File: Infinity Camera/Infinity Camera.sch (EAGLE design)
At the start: 6 parts

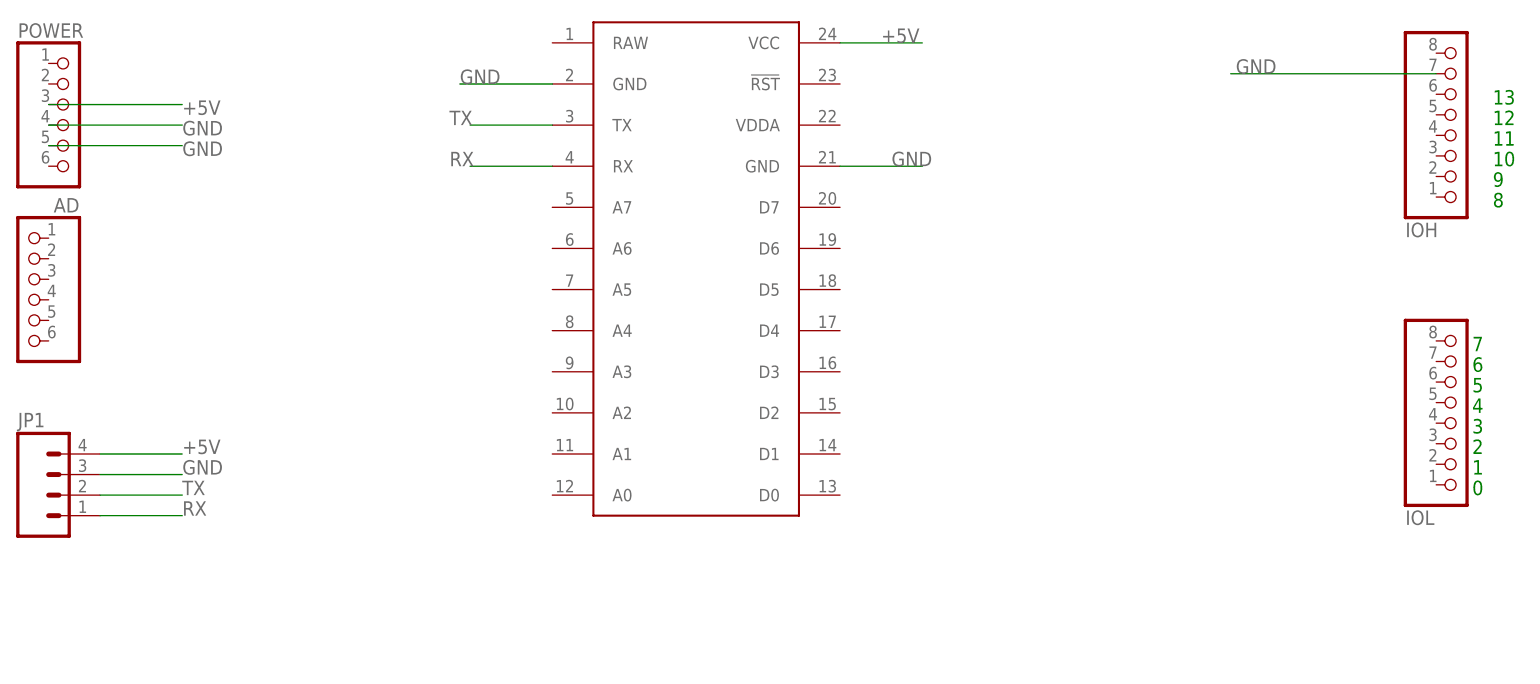
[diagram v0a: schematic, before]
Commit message: Reviewed Infinity Camera
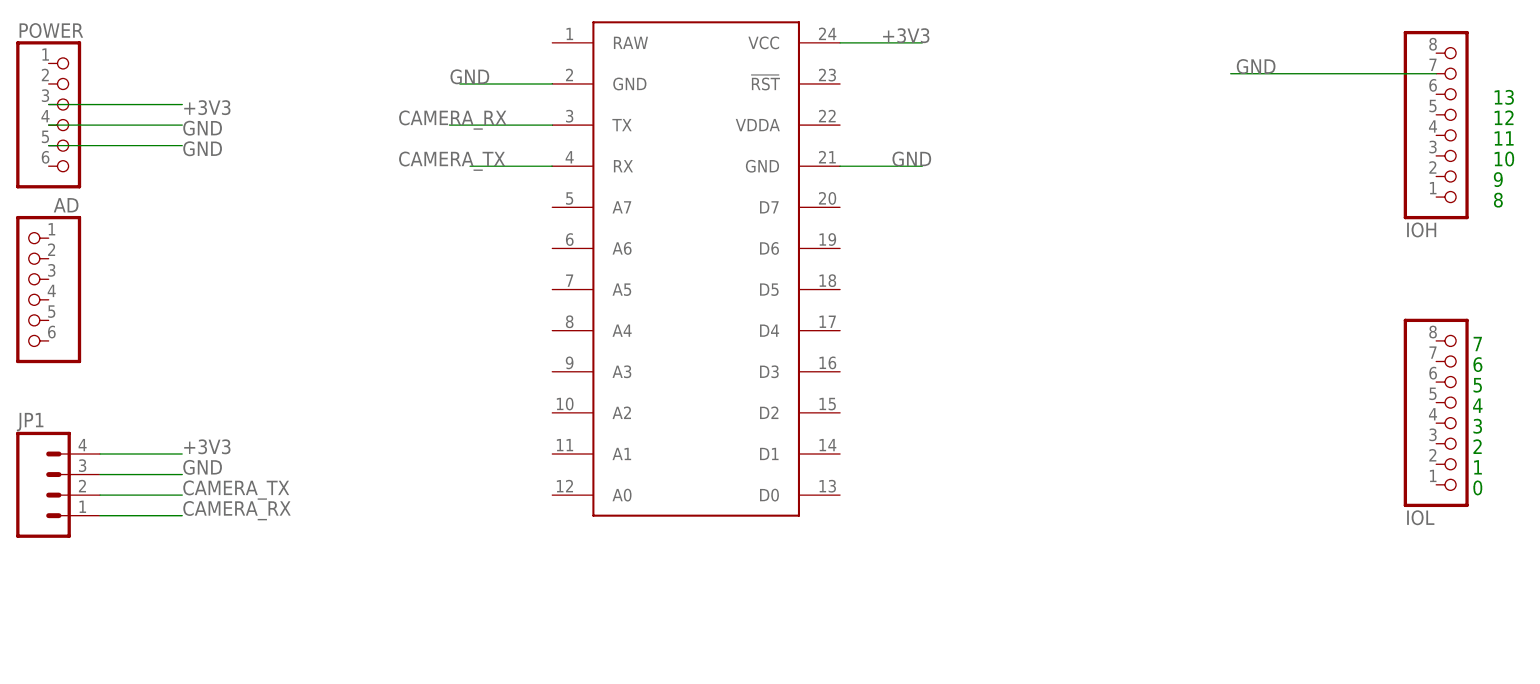
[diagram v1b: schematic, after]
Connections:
- net +5V renamed +3V3
- removed net RX: JP1.1, U$1.RX
- removed net TX: JP1.2, U$1.TX
- new net CAMERA_RX: JP1.1, U$1.TX
- new net CAMERA_TX: JP1.2, U$1.RX
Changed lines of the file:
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@@
 <setting verticaltext="up"/>
 </settings>
-<grid distance="0.1" unitdist="inch" unit="inch" style="lines" multiple="1" display="no" altdistance="0.01" altunitdist="inch" altunit="inch"/>
+<grid distance="0.05" unitdist="inch" unit="inch" style="lines" multiple="1" display="yes" altdistance="0.005" altunitdist="inch" altunit="inch"/>
 <layers>
 <layer number="1" name="Top" color="4" fill="1" visible="no" active="no"/>
@@
 <pinref part="U$1" gate="G$1" pin="GND@2"/>
 <wire x1="91.44" y1="88.9" x2="80.01" y2="88.9" width="0.1524" layer="91"/>
-<label x="80.01" y="88.9" size="1.778" layer="95"/>
+<label x="78.74" y="88.9" size="1.778" layer="95"/>
 </segment>
 <segment>
@@
 <segment>
 <pinref part="JP1" gate="G$1" pin="3"/>
-<wire x1="35.56" y1="40.64" x2="45.72" y2="40.64" width="0.2032" layer="91"/>
+<wire x1="35.56" y1="40.64" x2="45.72" y2="40.64" width="0.1524" layer="91"/>
 <label x="45.72" y="40.64" size="1.778" layer="95"/>
 </segment>
 </net>
-<net name="+5V" class="0">
+<net name="+3V3" class="0">
 <segment>
 <wire x1="29.21" y1="86.36" x2="45.72" y2="86.36" width="0.1524" layer="91"/>
@@
 <segment>
 <pinref part="JP1" gate="G$1" pin="4"/>
-<wire x1="35.56" y1="43.18" x2="45.72" y2="43.18" width="0.2032" layer="91"/>
+<wire x1="35.56" y1="43.18" x2="45.72" y2="43.18" width="0.1524" layer="91"/>
 <label x="45.72" y="43.18" size="1.778" layer="95"/>
 </segment>
 </net>
-<net name="TX" class="0">
+<net name="CAMERA_TX" class="0">
 <segment>
 <pinref part="JP1" gate="G$1" pin="2"/>
-<wire x1="35.56" y1="38.1" x2="45.72" y2="38.1" width="0.2032" layer="91"/>
+<wire x1="35.56" y1="38.1" x2="45.72" y2="38.1" width="0.1524" layer="91"/>
 <label x="45.72" y="38.1" size="1.778" layer="95"/>
 </segment>
 <segment>
+<pinref part="U$1" gate="G$1" pin="RX"/>
+<wire x1="91.44" y1="78.74" x2="81.28" y2="78.74" width="0.1524" layer="91"/>
+<label x="72.39" y="78.74" size="1.778" layer="95"/>
+</segment>
+</net>
+<net name="CAMERA_RX" class="0">
+<segment>
+<pinref part="JP1" gate="G$1" pin="1"/>
+<wire x1="35.56" y1="35.56" x2="45.72" y2="35.56" width="0.1524" layer="91"/>
+<label x="45.72" y="35.56" size="1.778" layer="95"/>
+</segment>
+<segment>
 <pinref part="U$1" gate="G$1" pin="TX"/>
-<wire x1="91.44" y1="83.82" x2="81.28" y2="83.82" width="0.2032" layer="91"/>
-<label x="78.74" y="83.82" size="1.778" layer="95"/>
-</segment>
-</net>
-<net name="RX" class="0">
-<segment>
-<pinref part="JP1" gate="G$1" pin="1"/>
-<wire x1="35.56" y1="35.56" x2="45.72" y2="35.56" width="0.2032" layer="91"/>
-<label x="45.72" y="35.56" size="1.778" layer="95"/>
-</segment>
-<segment>
-<pinref part="U$1" gate="G$1" pin="RX"/>
-<wire x1="91.44" y1="78.74" x2="81.28" y2="78.74" width="0.2032" layer="91"/>
-<label x="78.74" y="78.74" size="1.778" layer="95"/>
-</segment>
-</net>
+<wire x1="91.44" y1="83.82" x2="78.74" y2="83.82" width="0.1524" layer="91"/>
+<label x="72.39" y="83.82" size="1.778" layer="95"/>
+</segment>
+</net>

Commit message: Started adding transistor to the Inifinity Camera.  Still needs to be finished.  Generated Gerber files for the LCD Shield and had it spun up.  Infinity camera gerber files need to be updated upon completion
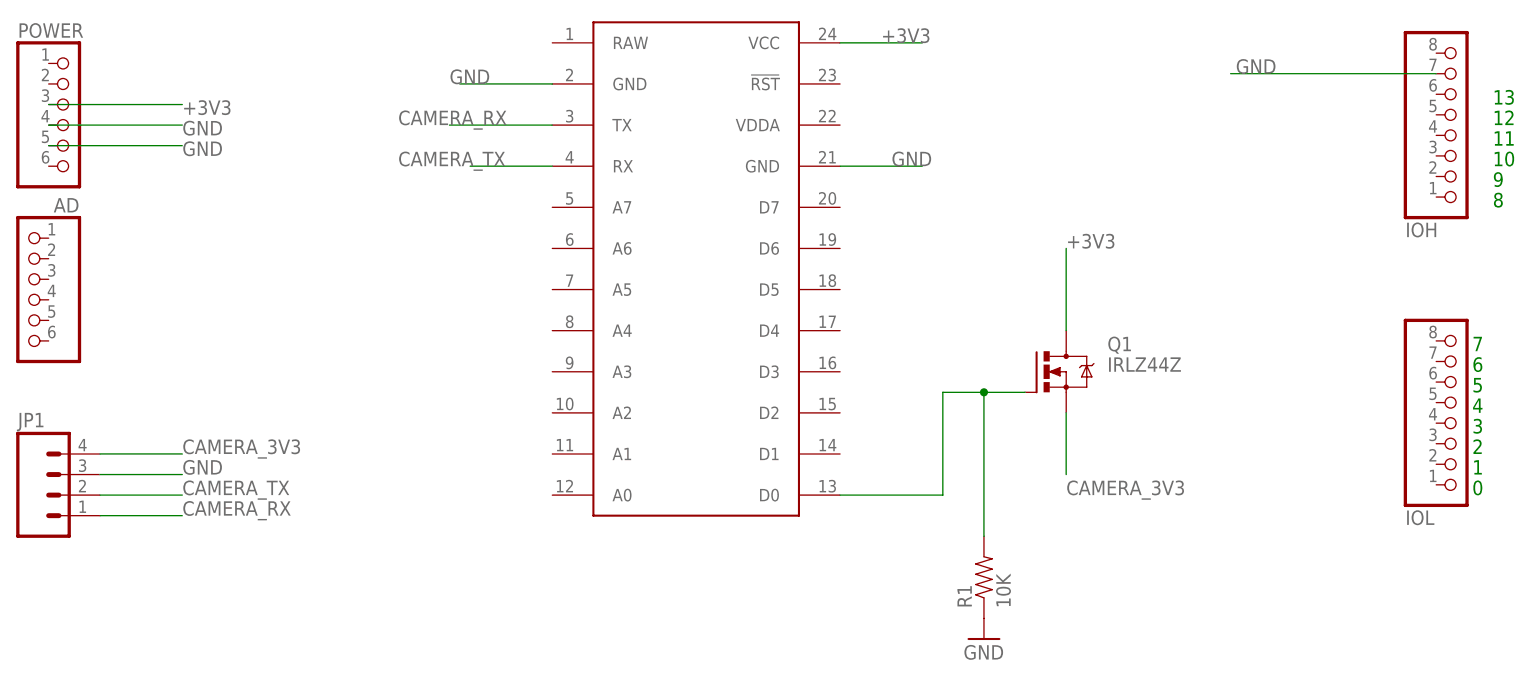
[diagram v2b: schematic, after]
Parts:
- added Q1: IRLZ44Z, transistor-power:IRLZ44Z
- added R1: 10K, SparkFun-Resistors:RESISTORPTH-1/4W
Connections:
- new net CAMERA_3V3: JP1.4, Q1.S
- new net N$1: Q1.G, R1.2, U$1.D0
- net +3V3: now also Q1.D; no longer JP1.4
- net GND: now also R1.1
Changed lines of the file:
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@@
 <setting verticaltext="up"/>
 </settings>
-<grid distance="0.05" unitdist="inch" unit="inch" style="lines" multiple="1" display="yes" altdistance="0.005" altunitdist="inch" altunit="inch"/>
+<grid distance="0.1" unitdist="inch" unit="inch" style="lines" multiple="1" display="no" altdistance="0.01" altunitdist="inch" altunit="inch"/>
 <layers>
 <layer number="1" name="Top" color="4" fill="1" visible="no" active="no"/>
@@
 <part name="U$1" library="Spark" deviceset="SPARK_CORE" device="CORE"/>
 <part name="JP1" library="SparkFun-Connectors" deviceset="M04" device="1.27MM"/>
+<part name="Q1" library="transistor-power" deviceset="IRLZ44Z" device=""/>
+<part name="R1" library="SparkFun-Resistors" deviceset="RESISTOR" device="PTH-1/4W" value="10K"/>
+<part name="GND1" library="SparkFun-Aesthetics" deviceset="GND" device=""/>
 </parts>
 <sheets>
@@
 <instance part="U$1" gate="G$1" x="109.22" y="66.04"/>
 <instance part="JP1" gate="G$1" x="30.48" y="38.1"/>
+<instance part="Q1" gate="G$1" x="152.4" y="53.34"/>
+<instance part="R1" gate="G$1" x="144.78" y="27.94" rot="R90"/>
+<instance part="GND1" gate="1" x="144.78" y="20.32"/>
 </instances>
 <busses>
@@
 <label x="45.72" y="40.64" size="1.778" layer="95"/>
 </segment>
+<segment>
+<pinref part="R1" gate="G$1" pin="1"/>
+<pinref part="GND1" gate="1" pin="GND"/>
+</segment>
 </net>
 <net name="+3V3" class="0">
@@
 </segment>
 <segment>
+<pinref part="Q1" gate="G$1" pin="D"/>
+<wire x1="154.94" y1="58.42" x2="154.94" y2="68.58" width="0.2032" layer="91"/>
+<label x="154.94" y="68.58" size="1.778" layer="95"/>
+</segment>
+</net>
+<net name="CAMERA_TX" class="0">
+<segment>
+<pinref part="JP1" gate="G$1" pin="2"/>
+<wire x1="35.56" y1="38.1" x2="45.72" y2="38.1" width="0.1524" layer="91"/>
+<label x="45.72" y="38.1" size="1.778" layer="95"/>
+</segment>
+<segment>
+<pinref part="U$1" gate="G$1" pin="RX"/>
+<wire x1="91.44" y1="78.74" x2="81.28" y2="78.74" width="0.1524" layer="91"/>
+<label x="72.39" y="78.74" size="1.778" layer="95"/>
+</segment>
+</net>
+<net name="CAMERA_RX" class="0">
+<segment>
+<pinref part="JP1" gate="G$1" pin="1"/>
+<wire x1="35.56" y1="35.56" x2="45.72" y2="35.56" width="0.1524" layer="91"/>
+<label x="45.72" y="35.56" size="1.778" layer="95"/>
+</segment>
+<segment>
+<pinref part="U$1" gate="G$1" pin="TX"/>
+<wire x1="91.44" y1="83.82" x2="78.74" y2="83.82" width="0.1524" layer="91"/>
+<label x="72.39" y="83.82" size="1.778" layer="95"/>
+</segment>
+</net>
+<net name="N$1" class="0">
+<segment>
+<pinref part="U$1" gate="G$1" pin="D0"/>
+<wire x1="127" y1="38.1" x2="139.7" y2="38.1" width="0.2032" layer="91"/>
+<wire x1="139.7" y1="38.1" x2="139.7" y2="50.8" width="0.2032" layer="91"/>
+<pinref part="Q1" gate="G$1" pin="G"/>
+<wire x1="139.7" y1="50.8" x2="144.78" y2="50.8" width="0.2032" layer="91"/>
+<wire x1="144.78" y1="50.8" x2="149.86" y2="50.8" width="0.2032" layer="91"/>
+<wire x1="144.78" y1="50.8" x2="144.78" y2="33.02" width="0.2032" layer="91"/>
+<junction x="144.78" y="50.8"/>
+<pinref part="R1" gate="G$1" pin="2"/>
+</segment>
+</net>
+<net name="CAMERA_3V3" class="0">
+<segment>
 <pinref part="JP1" gate="G$1" pin="4"/>
 <wire x1="35.56" y1="43.18" x2="45.72" y2="43.18" width="0.1524" layer="91"/>
 <label x="45.72" y="43.18" size="1.778" layer="95"/>
 </segment>
-</net>
-<net name="CAMERA_TX" class="0">
-<segment>
-<pinref part="JP1" gate="G$1" pin="2"/>
-<wire x1="35.56" y1="38.1" x2="45.72" y2="38.1" width="0.1524" layer="91"/>
-<label x="45.72" y="38.1" size="1.778" layer="95"/>
-</segment>
-<segment>
-<pinref part="U$1" gate="G$1" pin="RX"/>
-<wire x1="91.44" y1="78.74" x2="81.28" y2="78.74" width="0.1524" layer="91"/>
-<label x="72.39" y="78.74" size="1.778" layer="95"/>
-</segment>
-</net>
-<net name="CAMERA_RX" class="0">
-<segment>
-<pinref part="JP1" gate="G$1" pin="1"/>
-<wire x1="35.56" y1="35.56" x2="45.72" y2="35.56" width="0.1524" layer="91"/>
-<label x="45.72" y="35.56" size="1.778" layer="95"/>
-</segment>
-<segment>
-<pinref part="U$1" gate="G$1" pin="TX"/>
-<wire x1="91.44" y1="83.82" x2="78.74" y2="83.82" width="0.1524" layer="91"/>
-<label x="72.39" y="83.82" size="1.778" layer="95"/>
-</segment>
-</net>
+<segment>
+<pinref part="Q1" gate="G$1" pin="S"/>
+<wire x1="154.94" y1="48.26" x2="154.94" y2="40.64" width="0.2032" layer="91"/>
+<label x="154.94" y="38.1" size="1.778" layer="95"/>
+</segment>
+</net>

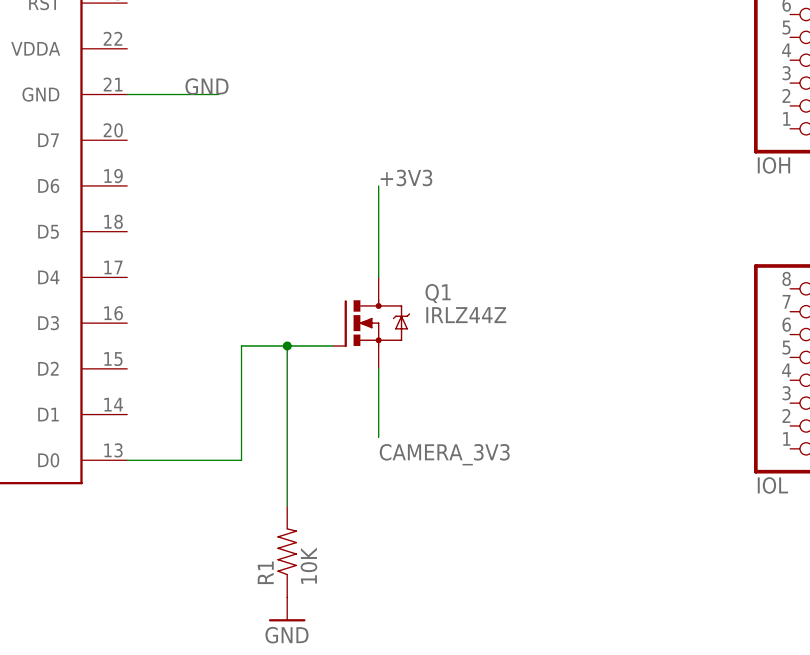
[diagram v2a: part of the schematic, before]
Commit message: Updated infinity camera with transistor and recreated Gerber files
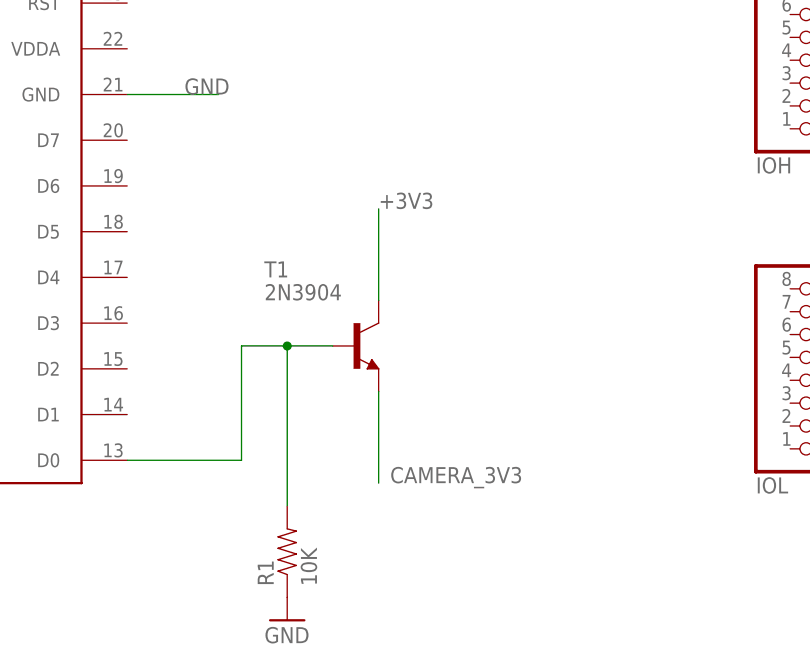
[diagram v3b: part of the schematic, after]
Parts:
- removed Q1: IRLZ44Z, transistor-power:IRLZ44Z
- added T1: 2N3904, transistor:2N3904
- JP1: device SparkFun-Connectors:M041.27MM -> SparkFun-Connectors:M04PTH
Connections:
- net +3V3: now also T1.C; no longer Q1.D
- net CAMERA_3V3: now also T1.E; no longer Q1.S
- net N$1: now also T1.B; no longer Q1.G
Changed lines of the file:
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@@
 <part name="POWER" library="pinhead" deviceset="PINHD-1X6" device=""/>
 <part name="U$1" library="Spark" deviceset="SPARK_CORE" device="CORE"/>
-<part name="JP1" library="SparkFun-Connectors" deviceset="M04" device="1.27MM"/>
-<part name="Q1" library="transistor-power" deviceset="IRLZ44Z" device=""/>
+<part name="JP1" library="SparkFun-Connectors" deviceset="M04" device="PTH"/>
 <part name="R1" library="SparkFun-Resistors" deviceset="RESISTOR" device="PTH-1/4W" value="10K"/>
 <part name="GND1" library="SparkFun-Aesthetics" deviceset="GND" device=""/>
+<part name="T1" library="transistor" deviceset="2N3904" device=""/>
 </parts>
 <sheets>
@@
 <instance part="U$1" gate="G$1" x="109.22" y="66.04"/>
 <instance part="JP1" gate="G$1" x="30.48" y="38.1"/>
-<instance part="Q1" gate="G$1" x="152.4" y="53.34"/>
 <instance part="R1" gate="G$1" x="144.78" y="27.94" rot="R90"/>
 <instance part="GND1" gate="1" x="144.78" y="20.32"/>
+<instance part="T1" gate="G1" x="152.4" y="50.8"/>
 </instances>
 <busses>
@@
 </segment>
 <segment>
-<pinref part="Q1" gate="G$1" pin="D"/>
-<wire x1="154.94" y1="58.42" x2="154.94" y2="68.58" width="0.2032" layer="91"/>
-<label x="154.94" y="68.58" size="1.778" layer="95"/>
+<wire x1="154.94" y1="55.88" x2="154.94" y2="66.04" width="0.1524" layer="91"/>
+<label x="154.94" y="66.04" size="1.778" layer="95"/>
+<pinref part="T1" gate="G1" pin="C"/>
 </segment>
 </net>
@@
 <segment>
 <pinref part="U$1" gate="G$1" pin="D0"/>
-<wire x1="127" y1="38.1" x2="139.7" y2="38.1" width="0.2032" layer="91"/>
-<wire x1="139.7" y1="38.1" x2="139.7" y2="50.8" width="0.2032" layer="91"/>
-<pinref part="Q1" gate="G$1" pin="G"/>
-<wire x1="139.7" y1="50.8" x2="144.78" y2="50.8" width="0.2032" layer="91"/>
-<wire x1="144.78" y1="50.8" x2="149.86" y2="50.8" width="0.2032" layer="91"/>
-<wire x1="144.78" y1="50.8" x2="144.78" y2="33.02" width="0.2032" layer="91"/>
+<wire x1="127" y1="38.1" x2="139.7" y2="38.1" width="0.1524" layer="91"/>
+<wire x1="139.7" y1="38.1" x2="139.7" y2="50.8" width="0.1524" layer="91"/>
+<wire x1="139.7" y1="50.8" x2="144.78" y2="50.8" width="0.1524" layer="91"/>
+<wire x1="144.78" y1="50.8" x2="149.86" y2="50.8" width="0.1524" layer="91"/>
+<wire x1="144.78" y1="50.8" x2="144.78" y2="33.02" width="0.1524" layer="91"/>
 <junction x="144.78" y="50.8"/>
 <pinref part="R1" gate="G$1" pin="2"/>
+<pinref part="T1" gate="G1" pin="B"/>
 </segment>
 </net>
@@
 </segment>
 <segment>
-<pinref part="Q1" gate="G$1" pin="S"/>
-<wire x1="154.94" y1="48.26" x2="154.94" y2="40.64" width="0.2032" layer="91"/>
-<label x="154.94" y="38.1" size="1.778" layer="95"/>
+<wire x1="154.94" y1="45.72" x2="154.94" y2="35.56" width="0.1524" layer="91"/>
+<label x="156.21" y="35.56" size="1.778" layer="95"/>
+<pinref part="T1" gate="G1" pin="E"/>
 </segment>
 </net>
